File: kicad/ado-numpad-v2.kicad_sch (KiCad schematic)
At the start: 39 parts, among them J1 Conn_01x04, J2 AudioJack4, SW1 SW_Push, SW10 SW_Push, SW11 SW_Push, SW12 SW_Push, SW13 SW_Push, SW14 SW_Push, SW15 SW_Push, SW16 SW_Push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

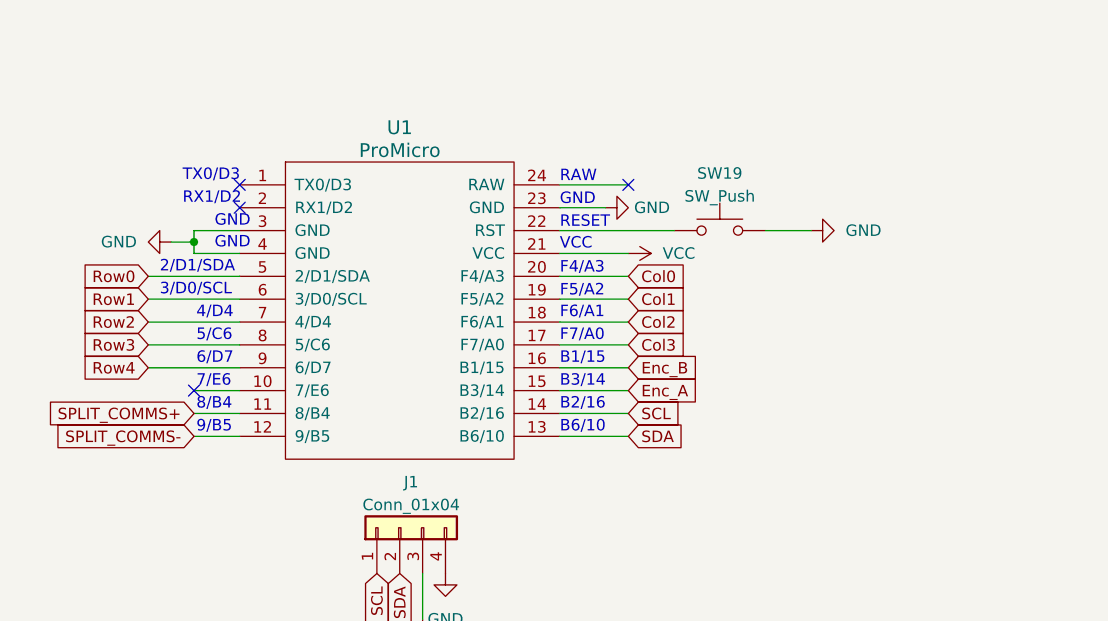
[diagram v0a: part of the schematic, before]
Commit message: Update to use 2 1x12_P2.54mm Pin Sockets
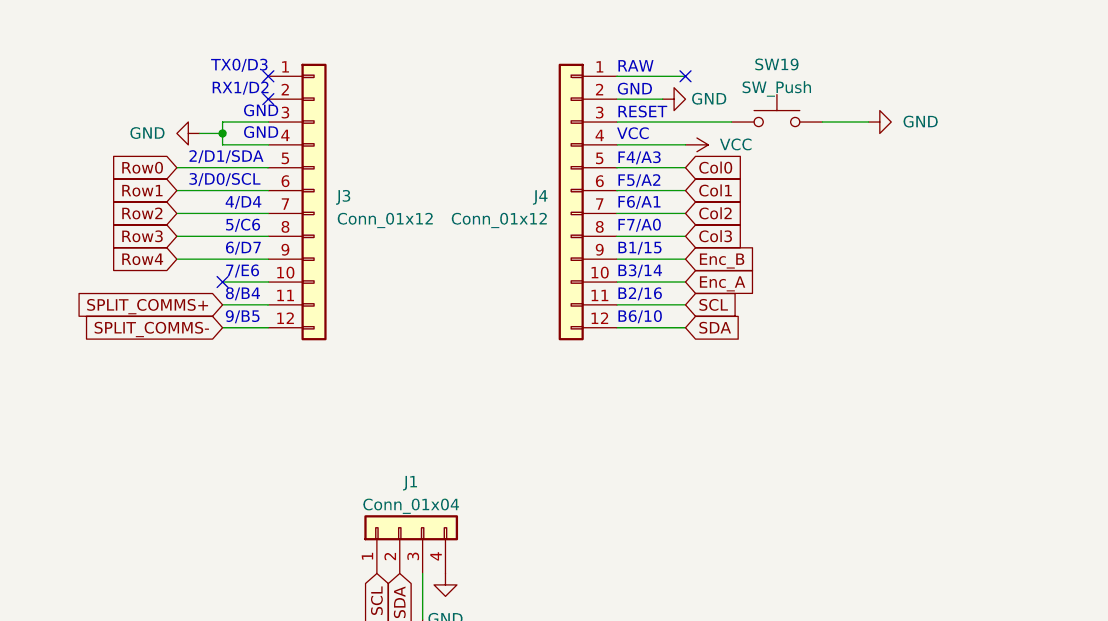
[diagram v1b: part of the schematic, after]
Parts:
- removed U1: ProMicro, kbd:ProMicro_v2_1side, symbol kbd:ProMicro
- added J3, J4: Conn_01x12, Connector_PinSocket_2.54mm:PinSocket_1x12_P2.54mm_Vertical, symbol Connector_Generic:Conn_01x12
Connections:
- net Col0: now also J4.5 (Pin_5)
- net Col1: now also J4.6 (Pin_6)
- net Col2: now also J4.7 (Pin_7)
- net Col3: now also J4.8 (Pin_8)
- net Enc_A: now also J4.10 (Pin_10)
- net Enc_B: now also J4.9 (Pin_9)
- net GND: now also J3.3 (Pin_3), J3.4 (Pin_4), J4.2 (Pin_2)
- net Row0: now also J3.5 (Pin_5)
- net Row1: now also J3.6 (Pin_6)
- net Row2: now also J3.7 (Pin_7)
- net Row3: now also J3.8 (Pin_8)
- net Row4: now also J3.9 (Pin_9)
- net SCL: now also J4.11 (Pin_11)
- net SDA: now also J4.12 (Pin_12)
- net SPLIT_COMMS+: now also J3.11 (Pin_11)
- net SPLIT_COMMS-: now also J3.12 (Pin_12)
- net VCC: now also J4.4 (Pin_4)
- net at SW19.2: now also J4.3 (Pin_3)
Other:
- moved on the sheet: SW19

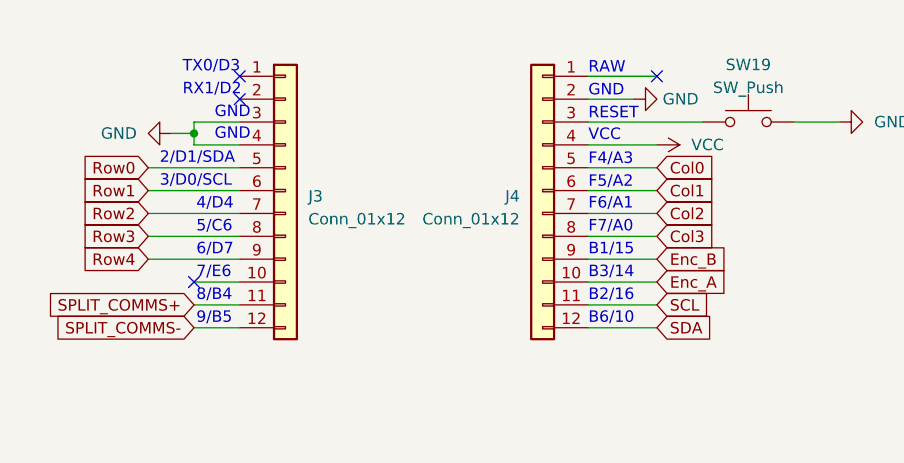
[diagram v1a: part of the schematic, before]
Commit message: Move Enc pins to Pin 1 and 2 on Pro Micro
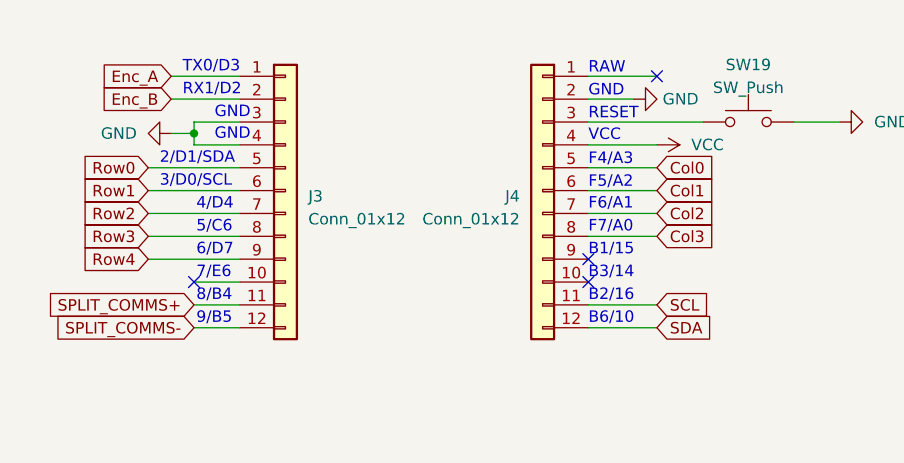
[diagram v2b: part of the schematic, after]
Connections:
- net Enc_A: now also J3.1 (Pin_1); no longer J4.10 (Pin_10)
- net Enc_B: now also J3.2 (Pin_2); no longer J4.9 (Pin_9)
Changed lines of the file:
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@@
   (junction (at 215.9 71.12) (diameter 0) (color 0 0 0 0)
   )
-  (no_connect (at 38.735 33.655))
-  (no_connect (at 38.735 36.195))
+  (no_connect (at 77.47 53.975))
+  (no_connect (at 77.47 56.515))
   (no_connect (at 33.655 56.515))
   (no_connect (at 85.09 33.655))
@@
     (stroke (width 0) (type default))
   )
-  (wire (pts (xy 85.09 53.975) (xy 77.47 53.975))
+  (wire (pts (xy 31.115 33.655) (xy 38.735 33.655))
     (stroke (width 0) (type default))
   )
@@
     (stroke (width 0) (type default))
   )
-  (wire (pts (xy 77.47 56.515) (xy 85.09 56.515))
+  (wire (pts (xy 38.735 36.195) (xy 31.115 36.195))
     (stroke (width 0) (type default))
   )
@@
     )
   )
-  (global_label "Enc_A" (shape input) (at 85.09 56.515 0) (fields_autoplaced)
-    (effects (font (size 1.27 1.27)) (justify left))
-    (property "Intersheetrefs" "${INTERSHEET_REFS}" (at 93.4386 56.515 0)
-      (effects (font (size 1.27 1.27)) (justify left) hide)
+  (global_label "Enc_A" (shape input) (at 31.115 33.655 180) (fields_autoplaced)
+    (effects (font (size 1.27 1.27)) (justify right))
+    (property "Intersheetrefs" "${INTERSHEET_REFS}" (at 22.7664 33.655 0)
+      (effects (font (size 1.27 1.27)) (justify right) hide)
     )
   )
@@
     )
   )
-  (global_label "Enc_B" (shape input) (at 85.09 53.975 0) (fields_autoplaced)
-    (effects (font (size 1.27 1.27)) (justify left))
-    (property "Intersheetrefs" "${INTERSHEET_REFS}" (at 93.62 53.975 0)
-      (effects (font (size 1.27 1.27)) (justify left) hide)
-    )
-  )
+  (global_label "Enc_B" (shape input) (at 31.115 36.195 180) (fields_autoplaced)
+    (effects (font (size 1.27 1.27)) (justify right))
+    (property "Intersheetrefs" "${INTERSHEET_REFS}" (at 22.585 36.195 0)
+      (effects (font (size 1.27 1.27)) (justify right) hide)
+    )
+  )
